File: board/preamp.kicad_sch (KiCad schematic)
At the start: 16 parts, among them U6 OPA2310

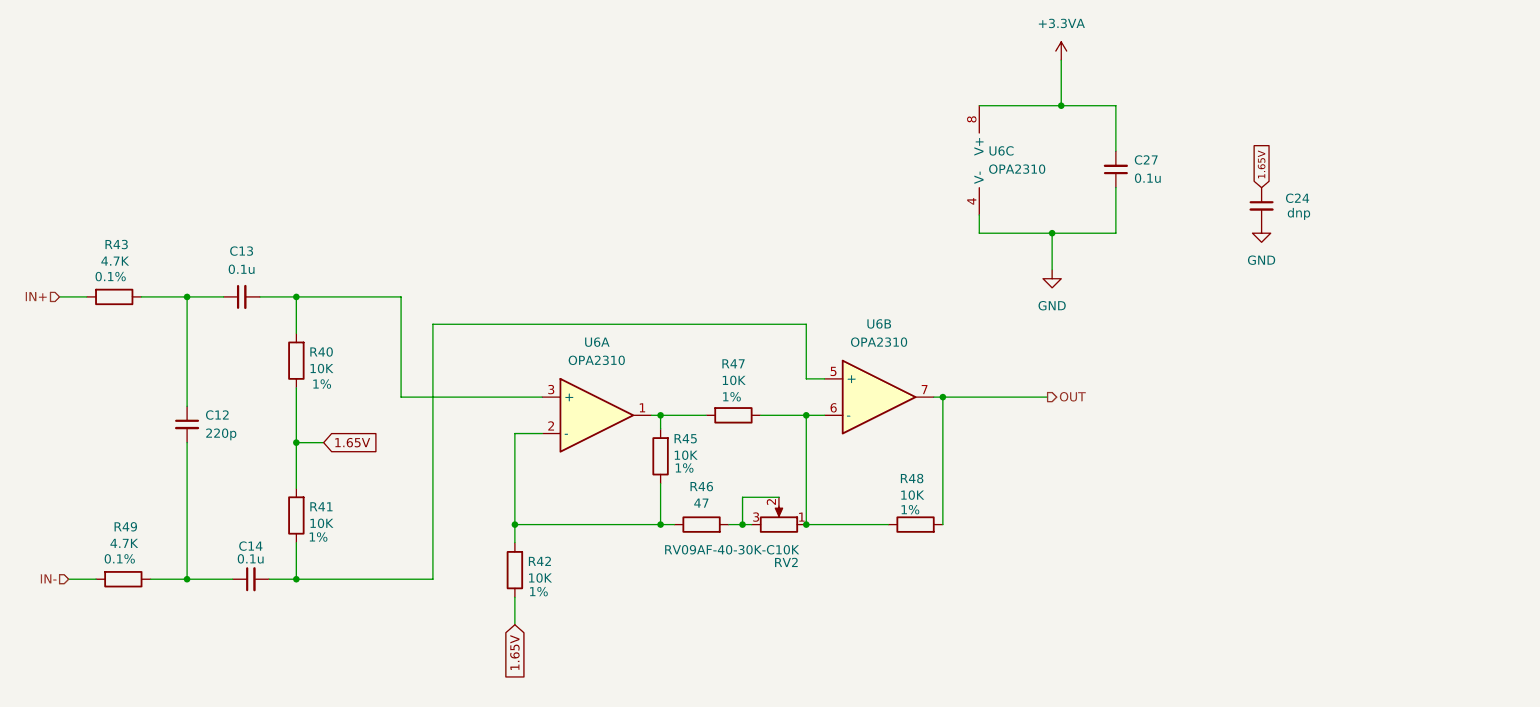
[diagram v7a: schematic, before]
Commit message: version 1.1c
- Fix misaligned traces at C16, C7 and C24
- Add missing Silkscreen value for C29
- Power switch 1mm further inside (sticks out quite a lot)
- more clearence for headphone jacks so that it is more difficult to bridge them to GND
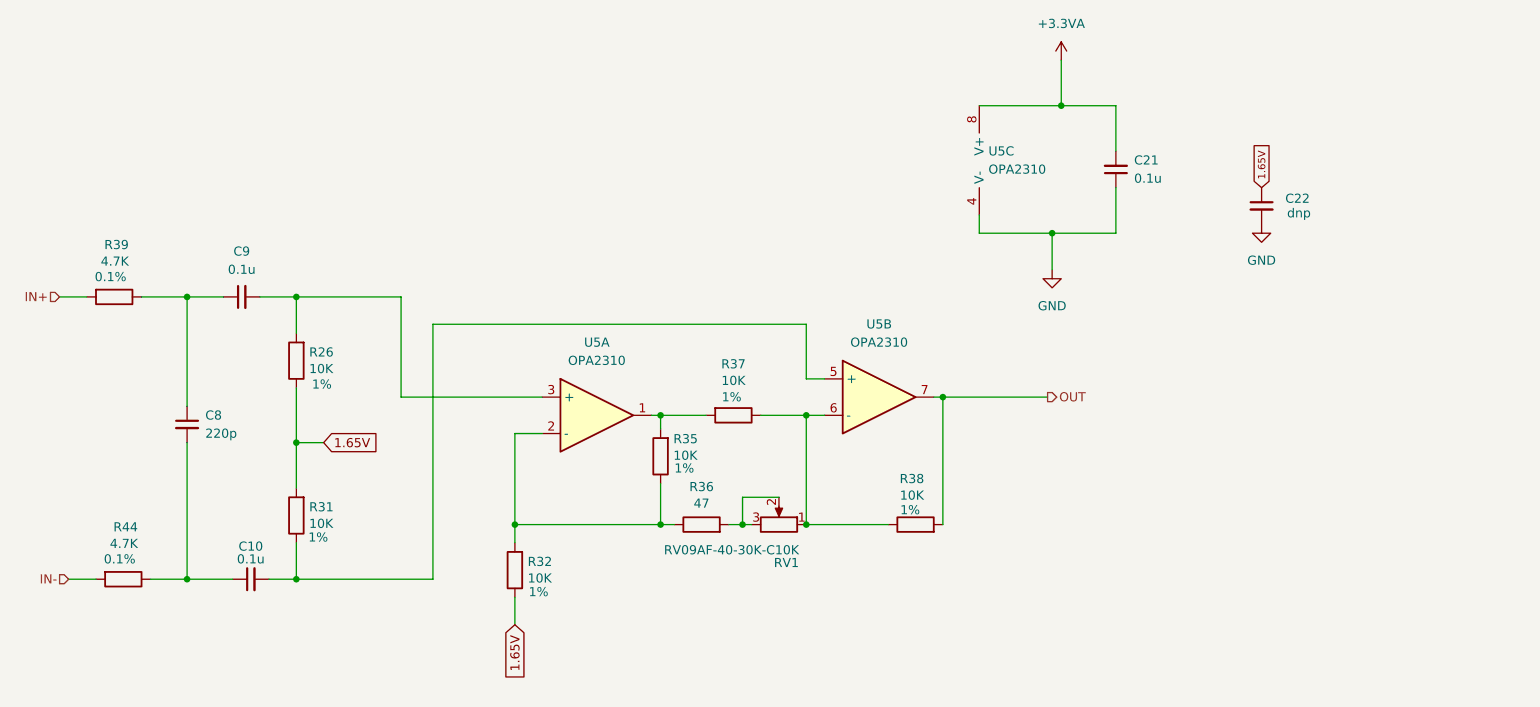
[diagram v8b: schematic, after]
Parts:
- renumbered C14 to C10, C27 to C21, C24 to C22, C12 to C8, C13 to C9, R40 to R26, R41 to R31, R42 to R32, R45 to R35, R46 to R36, R47 to R37, R48 to R38, R43 to R39, R49 to R44, RV2 to RV1, U6 to U5
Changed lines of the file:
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@@
 (kicad_sch
-	(version 20231120)
+	(version 20250114)
 	(generator "eeschema")
-	(generator_version "8.0")
+	(generator_version "9.0")
 	(paper "A4")
 	(junction
@@
 		(shape input)
 		(at 68.58 63.5 180)
-		(fields_autoplaced yes)
 		(effects
 			(font
@@
 		(shape output)
 		(at 206.375 77.47 0)
-		(fields_autoplaced yes)
 		(effects
 			(font
@@
 		(shape input)
 		(at 69.85 102.87 180)
-		(fields_autoplaced yes)
 		(effects
 			(font
@@
 		(dnp no)
 		(fields_autoplaced yes)
-		(property "Reference" "#PWR033"
+		(property "Reference" "#PWR024"
 			(at 236.22 59.69 0)
 			(effects
@@
 		(dnp no)
 		(fields_autoplaced yes)
-		(property "Reference" "#PWR042"
+		(property "Reference" "#PWR041"
 			(at 207.01 66.04 0)
 			(effects
@@
 		(on_board yes)
 		(dnp no)
-		(property "Reference" "R45"
+		(property "Reference" "R35"
 			(at 154.178 83.312 0)
 			(effects
@@
 		(on_board yes)
 		(dnp no)
-		(property "Reference" "RV2"
+		(property "Reference" "RV1"
 			(at 171.704 100.584 90)
 			(effects
@@
 		(on_board yes)
 		(dnp no)
-		(property "Reference" "R46"
+		(property "Reference" "R36"
 			(at 158.115 89.9922 90)
 			(effects
@@
 		(dnp no)
 		(fields_autoplaced yes)
-		(property "Reference" "#PWR038"
+		(property "Reference" "#PWR023"
 			(at 208.28 34.29 0)
 			(effects
@@
 		(on_board yes)
 		(dnp no)
-		(property "Reference" "R47"
+		(property "Reference" "R37"
 			(at 162.56 72.8726 90)
 			(effects
@@
 		(dnp no)
 		(fields_autoplaced yes)
-		(property "Reference" "U6"
+		(property "Reference" "U5"
 			(at 143.51 69.85 0)
 			(effects
@@
 		(on_board yes)
 		(dnp no)
-		(property "Reference" "R41"
+		(property "Reference" "R31"
 			(at 103.378 92.8116 0)
 			(effects
@@
 		(on_board yes)
 		(dnp no)
-		(property "Reference" "R40"
+		(property "Reference" "R26"
 			(at 103.378 71.2216 0)
 			(effects
@@
 		(on_board yes)
 		(dnp no)
-		(property "Reference" "R48"
+		(property "Reference" "R38"
 			(at 187.452 88.8746 90)
 			(effects
@@
 		(on_board yes)
 		(dnp no)
-		(property "Reference" "C14"
+		(property "Reference" "C10"
 			(at 95.25 98.298 90)
 			(effects
@@
 		(on_board yes)
 		(dnp no)
-		(property "Reference" "C24"
+		(property "Reference" "C22"
 			(at 239.522 49.784 0)
 			(effects
@@
 		(dnp no)
 		(fields_autoplaced yes)
-		(property "Reference" "C13"
+		(property "Reference" "C9"
 			(at 93.9863 57.15 90)
 			(effects
@@
 		(dnp no)
 		(fields_autoplaced yes)
-		(property "Reference" "U6"
+		(property "Reference" "U5"
 			(at 182.88 67.31 0)
 			(effects
@@
 		(on_board yes)
 		(dnp no)
-		(property "Reference" "R42"
+		(property "Reference" "R32"
 			(at 133.858 100.4316 0)
 			(effects
@@
 		(on_board yes)
 		(dnp no)
-		(property "Reference" "R43"
+		(property "Reference" "R39"
 			(at 78.232 56.2356 90)
 			(effects
@@
 		(dnp no)
 		(fields_autoplaced yes)
-		(property "Reference" "C27"
+		(property "Reference" "C21"
 			(at 218.44 44.4435 0)
 			(effects
@@
 		(dnp no)
 		(fields_autoplaced yes)
-		(property "Reference" "U6"
+		(property "Reference" "U5"
 			(at 198.12 43.1799 0)
 			(effects
@@
 		(on_board yes)
 		(dnp no)
-		(property "Reference" "C12"
+		(property "Reference" "C8"
 			(at 88.9 80.0163 0)
 			(effects
@@
 		(on_board yes)
 		(dnp no)
-		(property "Reference" "R49"
+		(property "Reference" "R44"
 			(at 79.502 95.6056 90)
 			(effects
